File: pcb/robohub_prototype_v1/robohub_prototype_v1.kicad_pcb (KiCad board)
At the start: 10 copper layers, 102 parts, among them J21 Barrel_Jack_Switch_Pin3Ring, J51 USB_A, J52 USB_A, J71 USB_A, U1 ATSAMA5D27C, U21 LM3880, U22 TPS564242DRL, U23 TPS564242DRL, U24 TPS564242DRL, U25 TPS564242DRL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

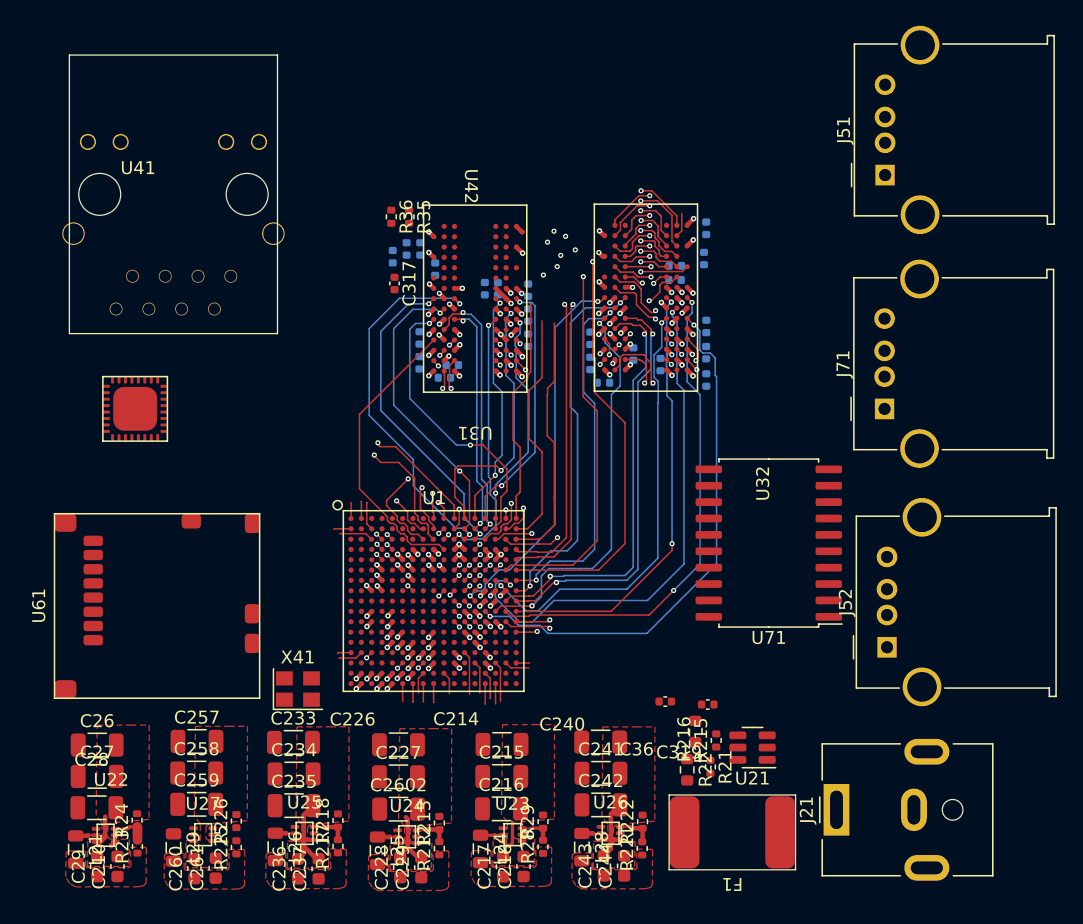
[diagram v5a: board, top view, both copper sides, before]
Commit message: Update footprint assignment. begin laying out ethernet
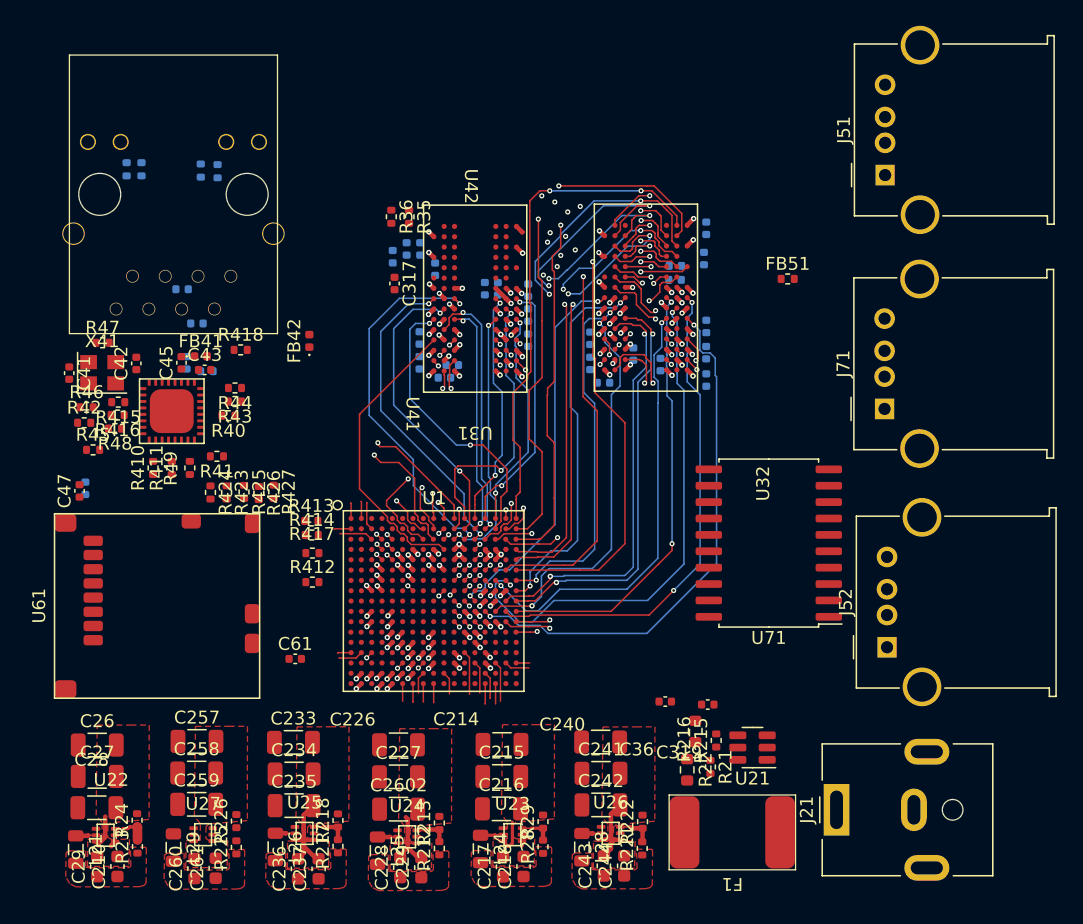
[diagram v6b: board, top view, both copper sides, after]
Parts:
- added C41: 22p, Capacitor_SMD:C_0402_1005Metric, F.Cu at (93.6, 77.0)
- added C410: 100n, Capacitor_SMD:C_0402_1005Metric, B.Cu at (102.3, 70.5)
- added C42: 22p, Capacitor_SMD:C_0402_1005Metric, F.Cu at (98.8, 76.3)
- added C43: 2u2, Capacitor_SMD:C_0402_1005Metric, F.Cu at (104.1, 76.8)
- added C44: 100n, Capacitor_SMD:C_0402_1005Metric, B.Cu at (104.3, 76.9)
- added C45: 10u, Capacitor_SMD:C_0402_1005Metric, F.Cu at (102.3, 76.2)
- added C46: 100n, Capacitor_SMD:C_0402_1005Metric, B.Cu at (102.7, 76.2)
- added C47: 10u, Capacitor_SMD:C_0402_1005Metric, F.Cu at (94.4, 86.2)
- added C48: 100n, Capacitor_SMD:C_0402_1005Metric, B.Cu at (94.8, 86.0)
- added C49: 100n, Capacitor_SMD:C_0402_1005Metric, B.Cu at (103.5, 73.2)
- added C61: 10u, Capacitor_SMD:C_0402_1005Metric, F.Cu at (111.1, 99.2)
- added FB41: FerriteBead, Diode_SMD:D_0402_1005Metric, F.Cu at (103.8, 75.8)
- added FB42: FerriteBead, Diode_SMD:D_0402_1005Metric, F.Cu at (112.2, 74.5)
- added FB51: FerriteBead, Resistor_SMD:R_0402_1005Metric, F.Cu at (149.3, 69.8)
- added R40: 10K, Resistor_SMD:R_0402_1005Metric, F.Cu at (105.9, 80.3)
- added R41: 1K, Resistor_SMD:R_0402_1005Metric, F.Cu at (105.0, 83.5)
- added R410: 22, Resistor_SMD:R_0402_1005Metric, F.Cu at (100.1, 84.4)
- added R411: 39, Resistor_SMD:R_0402_1005Metric, F.Cu at (101.5, 84.4)
- added R412: 22, Resistor_SMD:R_0402_1005Metric, F.Cu at (112.5, 93.2)
- added R413: 22, Resistor_SMD:R_0402_1005Metric, F.Cu at (112.4, 88.5)
- added R414: 22, Resistor_SMD:R_0402_1005Metric, F.Cu at (112.4, 89.6)
- added R415: 22, Resistor_SMD:R_0402_1005Metric, F.Cu at (97.4, 79.3)
- added R416: 22, Resistor_SMD:R_0402_1005Metric, F.Cu at (97.3, 80.3)
- added R417: 22, Resistor_SMD:R_0402_1005Metric, F.Cu at (112.5, 91.0)
- added R418: 6k4, Resistor_SMD:R_0402_1005Metric, F.Cu at (106.9, 75.2)
- added R419: 10k, Resistor_SMD:R_0402_1005Metric, B.Cu at (99.2, 61.2)
- added R42: 1K, Resistor_SMD:R_0402_1005Metric, F.Cu at (94.8, 80.9)
- added R420: 10k, Resistor_SMD:R_0402_1005Metric, B.Cu at (103.8, 61.4)
- added R421: 510, Resistor_SMD:R_0402_1005Metric, B.Cu at (98.0, 61.2)
- added R422: 510, Resistor_SMD:R_0402_1005Metric, B.Cu at (105.1, 61.4)
- added R423: 10K, Resistor_SMD:R_0402_1005Metric, F.Cu at (105.8, 86.3)
- added R424: 10K, Resistor_SMD:R_0402_1005Metric, F.Cu at (104.5, 86.3)
- added R425: 10K, Resistor_SMD:R_0402_1005Metric, F.Cu at (107.2, 86.3)
- added R426: 10K, Resistor_SMD:R_0402_1005Metric, F.Cu at (108.3, 86.3)
- added R427: 10K, Resistor_SMD:R_0402_1005Metric, F.Cu at (109.5, 86.2)
- added R43: 10K, Resistor_SMD:R_0402_1005Metric, F.Cu at (106.5, 79.2)
- added R44: 10K, Resistor_SMD:R_0402_1005Metric, F.Cu at (106.5, 78.2)
- added R45: 10K, Resistor_SMD:R_0402_1005Metric, F.Cu at (95.5, 83.0)
- added R46: 10K, Resistor_SMD:R_0402_1005Metric, F.Cu at (95.0, 79.7)
- added R47: DNP, Resistor_SMD:R_0402_1005Metric, F.Cu at (96.2, 74.7)
- added R48: 22, Resistor_SMD:R_0402_1005Metric, F.Cu at (97.2, 81.3)
- added R49: 22, Resistor_SMD:R_0402_1005Metric, F.Cu at (103.0, 84.4)
- moved X41 28.8 mm to (96.2, 77.0)
- moved U41 2.85 mm to (101.5, 80.0), turned to -90 degrees
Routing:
- net /DDR2_3/DDR_A2: track 20.9 -> 38.5 mm, vias 1 -> 2
- net /DDR2_3/DDR_A12: track 22.0 -> 38.8 mm, vias 1 -> 2
- net /DDR2_3/DDR_A6: track 25.9 -> 41.0 mm, vias 2 -> 3
- net /DDR2_3/DDR_A1: track 22.6 -> 37.4 mm, vias 1 -> 2
- net /DDR2_3/DDR_A8: track 23.9 -> 38.7 mm, vias 2 -> 3
- net /DDR2_3/DDR_A7: track 34.2 -> 49.0 mm, vias 1 -> 2
- net /DDR2_3/DDR_A3: track 24.7 -> 39.1 mm, vias 2 -> 3
- net /DDR2_3/DDR_A11: track 19.1 -> 32.8 mm, vias 2 -> 3
- net /DDR2_3/DDR_A4: track 23.5 -> 37.1 mm, vias 2 -> 3
- net /DDR2_3/DDR_A9: track 28.0 -> 40.9 mm, vias 2 -> 3
- net /DDR2_3/DDR_A5: track 36.2 -> 47.3 mm, vias 2 -> 3
- net /DDR2_3/DDR_A13: track 40.2 -> 51.0 mm, vias 2 -> 3
- net /DDR2_3/DDR_A10: track 26.7 -> 36.0 mm, vias 2 -> 3
